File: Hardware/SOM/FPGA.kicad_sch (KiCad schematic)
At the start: 1 part, among them U1 LFE5UM5G-85F-8BG381x

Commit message: SOM: DDR schematics update
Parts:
- added C13, C14, C15, C16, C17, C19, C20, C21, C22, C23, C25, C26, C27, C28: 100nF, Capacitor_SMD:C_0402_1005Metric, symbol RA8M1:885012205092
- added C18, C24, C29, C30: 10uF, Capacitor_SMD:C_0402_1005Metric, symbol RA8M1:885012205092
- U1: value LFE5UM5G-85F-8BG381x -> LFE5UM5G-85F
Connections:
- net VCC_CORE: now reaches U1.H10 (VCC), U1.H11 (VCC), U1.H12 (VCC), U1.H13 (VCC), U1.H8 (VCC), U1.H9 (VCC), U1.J13 (VCC), U1.J8 (VCC), U1.K13 (VCC), U1.K8 (VCC), U1.L13 (VCC), U1.L8 (VCC), U1.M13 (VCC), U1.M8 (VCC), U1.N10 (VCC), U1.N11 (VCC), U1.N12 (VCC), U1.N13 (VCC), U1.N8 (VCC), U1.N9 (VCC)
- net VCC_CORE: now also C13.2, C15.2, C17.2, C19.2, C21.2, C23.2, C25.2, C26.2, C27.2, C28.2, C29.2, C30.2
- net 1.5V: now reaches U1.L14 (VCCIO3), U1.L15 (VCCIO3), U1.M15 (VCCIO3)
- net 1.5V: now also U1.H14 (VCCIO2), U1.H15 (VCCIO2), U1.J15 (VCCIO2), C14.2, C16.2, C18.2, C20.2, C22.2, C24.2
- net DDR_DQ0: now reaches U1.N19 (PR83A)
- net DDR_DQ1: now reaches U1.N20 (PR83B)
- net DDR_DQ3: now reaches U1.P18 (PR83D)
- net DDR_DQ2: now reaches U1.P19 (PR83C)
- net DDR_DQ4: now reaches U1.P20 (PR86A)
- net DDR_LDQS_P: now reaches U1.R18 (PR89B)
- net DDR_DQ5: now reaches U1.R20 (PR86B)
- net DDR_LDQS_N: now reaches U1.T19 (PR89A)
- net DDR_DQ6: now reaches U1.T20 (PR86C)
- net DDR_DQ7: now reaches U1.U20 (PR86D)
- net DDR_DQ8: now reaches U1.C20 (PR35A)
- net DDR_DQ9: now reaches U1.D19 (PR35B)
- net DDR_DQ10: now reaches U1.D20 (PR35C)
- net DDR_DQ11: now reaches U1.E19 (PR35D)
- net DDR_DQ12: now reaches U1.E20 (PR38A)
- net DDR_DQ13: now reaches U1.F19 (PR38B)
- net DDR_DQ14: now reaches U1.F20 (PR38C)
- net DDR_UDQS_N: now reaches U1.G19 (PR41A)
- net DDR_DQ15: now reaches U1.G20 (PR38D)
- net DDR_UDQS_P: now reaches U1.H20 (PR41B)
- net JTAG_TDI: now reaches U1.R5 (TDI)
- net JTAG_TCK: now reaches U1.T5 (TCK)
- net JTAG_TMS: now reaches U1.U5 (TMS)
- net JTAG_TDO: now reaches U1.V4 (TDO)
- new net GND: C13.1, C14.1, C15.1, C16.1, C17.1, C18.1, C19.1, C20.1, C21.1, C22.1, C23.1, C24.1, C25.1, C26.1, C27.1, C28.1, C29.1, C30.1
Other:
- note added: "FPGA Decoupling"
- note added: "FPGA: BANK-0"
- note added: "FPGA: BANK-1"
- note added: "FPGA: BANK-2"
- note added: "FPGA: BANK-3"
- note added: "FPGA: BANK-6"
- note added: "FPGA: BANK-7"
- note added: "FPGA: BANK-8"
- note added: "FPGA: DEBUG"
- note added: "VCCIO B2"
- note added: "VCCIO B3"
- moved on the sheet: U1A, U1B, U1C, U1D, U1E, U1F, U1G, U1H, U1I, U1J, U1K

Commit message: some schematics update
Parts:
- added C31, C32: 100nF, Capacitor_SMD:C_0402_1005Metric, symbol RA8M1:885012205092
- added C33: 10uF, Capacitor_SMD:C_0402_1005Metric, symbol RA8M1:885012205092
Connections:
- net 1.5V: now also C31.2, C32.2, C33.2
- net DDR_LDQS_N: now also U1.R18 (PR89B); no longer U1.T19 (PR89A)
- net DDR_LDQS_P: now also U1.T19 (PR89A); no longer U1.R18 (PR89B)
- net DDR_UDQS_N: now also U1.H20 (PR41B); no longer U1.G19 (PR41A)
- net DDR_UDQS_P: now also U1.G19 (PR41A); no longer U1.H20 (PR41B)
- net GND: now also C31.1, C32.1, C33.1
- net DDR_A1: now reaches U1.A15 (PT103A)
- net DDR_A6: now reaches U1.A16 (PT110A)
- net DDR_A12: now reaches U1.A17 (PT116A)
- net DDR_A14: now reaches U1.A18 (PT119A)
- net DDR_BA1: now reaches U1.A19 (PT121A)
- net DDR_A2: now reaches U1.B15 (PT105A)
- net DDR_A7: now reaches U1.B16 (PT110B)
- net DDR_A10: now reaches U1.B17 (PT114A)
- net DDR_A13: now reaches U1.B18 (PT116B)
- net DDR_BA0: now reaches U1.B19 (PT119B)
- net DDR_BA2: now reaches U1.B20 (PT121B)
- net DDR_A3: now reaches U1.C15 (PT105B)
- net DDR_A8: now reaches U1.C16 (PT112A)
- net DDR_A11: now reaches U1.C17 (PT114B)
- net DDR_A4: now reaches U1.D15 (PT107A)
- net DDR_A9: now reaches U1.D16 (PT112B)
- net DDR_A0: now reaches U1.E14 (PT85B)
- net DDR_A5: now reaches U1.E15 (PT107B)
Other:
- note added: "VCCIO B1"

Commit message: QSPI, banks IO decoupling
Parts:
- added C11, C12, C25, C26, C37, C38: 10uF, Capacitor_SMD:C_0402_1005Metric, symbol RA8M1:885012205092
- added C16, C17, C20, C21, C29, C3, C30, C33, C34, C4, C7, C8: 100nF, Capacitor_SMD:C_0402_1005Metric, symbol RA8M1:885012205092
- U1: MPN (none) -> LFE5UM5G-85F-8BG381I; Manufacturer (none) -> Lattice
- renumbered C13 to C1, C18 to C10, C19 to C13, C21 to C14, C20 to C15, C23 to C18, C22 to C19, C14 to C2, C25 to C22, C26 to C23, C31 to C28, C28 to C31, C29 to C35, C33 to C36, C30 to C39, C15 to C5, C16 to C6, C17 to C9
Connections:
- net 1.5V: now also U1.F11 (VCCIO1), U1.F12 (VCCIO1), C11.2, C3.2, C7.2; no longer C10.2, C2.2, C6.2
- net GND: now also C11.1, C12.1, C16.1, C17.1, C20.1, C21.1, C25.1, C26.1, C29.1, C3.1, C30.1, C33.1, C34.1, C37.1, C38.1, C4.1, C7.1, C8.1
- net 3.3V: now reaches U1.P10 (VCCIO8), U1.P9 (VCCIO8)
- net 3.3V: now also C30.2, C34.2, C38.2
- net VCC_CORE renamed 1.2V
- new net: C16.2, C20.2, C25.2
- new net: C29.2, C33.2, C37.2
- new net: C10.2, C2.2, C6.2
- new net: C12.2, C4.2, C8.2
- new net: C17.2, C21.2, C26.2
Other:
- note added: "VCCIO B0"
- note added: "VCCIO B4"
- note added: "VCCIO B5"
- note added: "VCCIO B6"
- note added: "VCCIO B7"
- note added: "VCCIO B8"

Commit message: QSPI connected
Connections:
- net QSPI_CLK: now also U1.U3 (CCLK)
- net QSPI_CS: now also U1.R2 (PB15A)
- net QSPI_MISO/DQ1: now also U1.V2 (PB11A)
- net QSPI_MOSI/DQ0: now also U1.W2 (PB11B)
- net QSPI_RST/DQ3: now also U1.W1 (PB9A)
- net QSPI_WP/DQ2: now also U1.Y2 (PB9B)

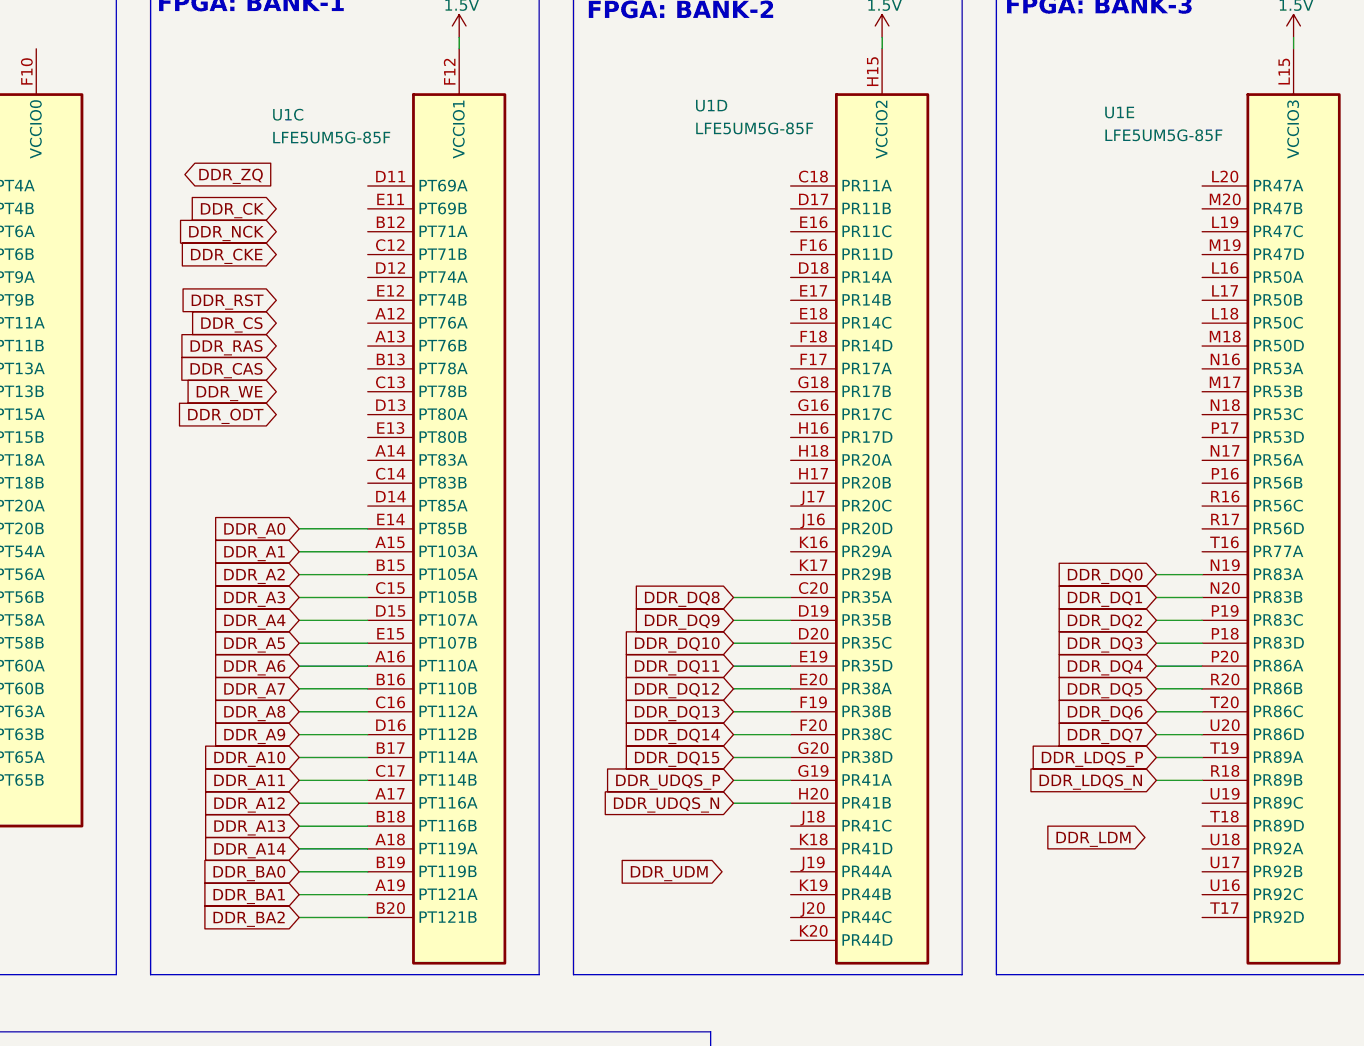
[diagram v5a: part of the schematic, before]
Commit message: DDR-FPGA connection
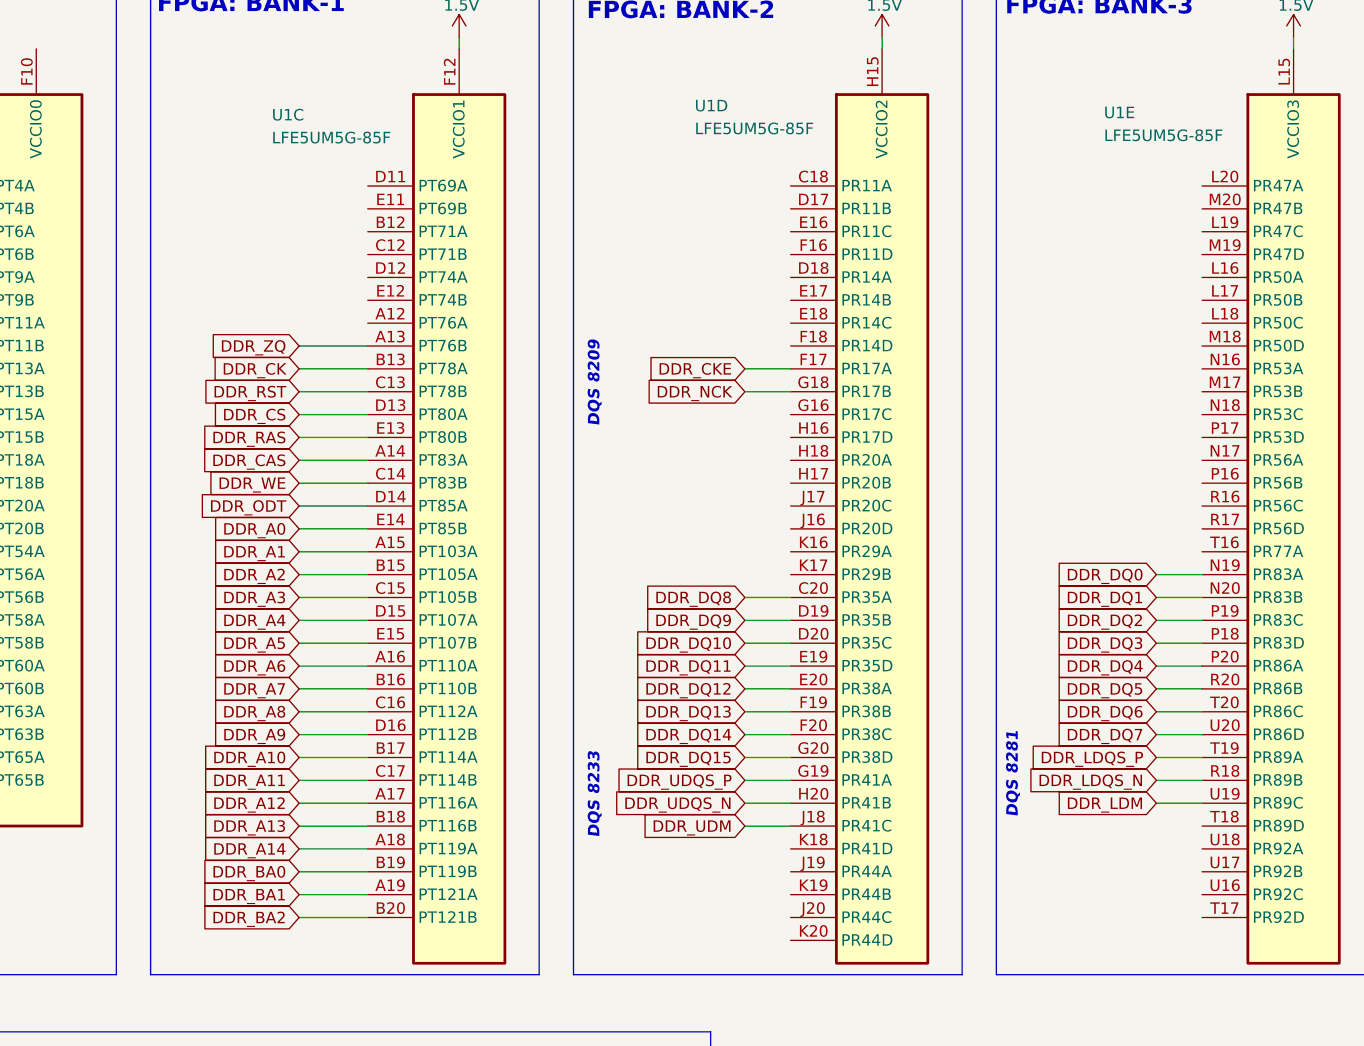
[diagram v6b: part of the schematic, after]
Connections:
- net DDR_CAS: now also U1.A14 (PT83A)
- net DDR_CK: now also U1.B13 (PT78A)
- net DDR_CKE: now also U1.F17 (PR17A)
- net DDR_CS: now also U1.D13 (PT80A)
- net DDR_LDM: now also U1.U19 (PR89C)
- net DDR_NCK: now also U1.G18 (PR17B)
- net DDR_ODT: now also U1.D14 (PT85A)
- net DDR_RAS: now also U1.E13 (PT80B)
- net DDR_RST: now also U1.C13 (PT78B)
- net DDR_UDM: now also U1.J18 (PR41C)
- net DDR_WE: now also U1.C14 (PT83B)
- net DDR_ZQ: now also U1.A13 (PT76B)
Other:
- note added: "DQS 8209"
- note added: "DQS 8233"
- note added: "DQS 8281"
